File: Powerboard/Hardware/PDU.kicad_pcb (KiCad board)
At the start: 4 copper layers, 60 x 50 mm, 127 parts, among them IC2 SiC437BED-T1-GE3, J1 Conn_01x03_MountingPin, J2 FAN, J3 USB_C_Receptacle_USB2.0, J4 Conn_01x02_Male, J5 Conn_01x08_Male, J6 Conn_01x02_Male, J7 XT60PW-M, J8 Conn_01x04_Male, J9 XT60PW-M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

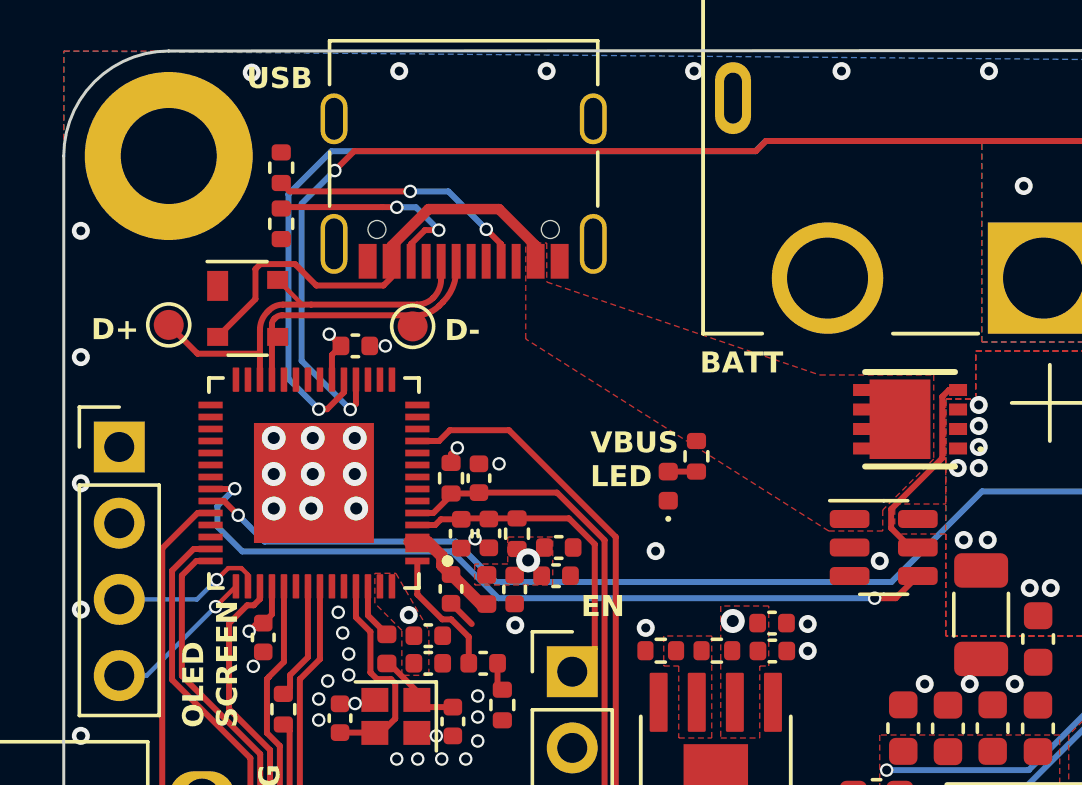
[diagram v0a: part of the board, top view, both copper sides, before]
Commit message: data lines fix
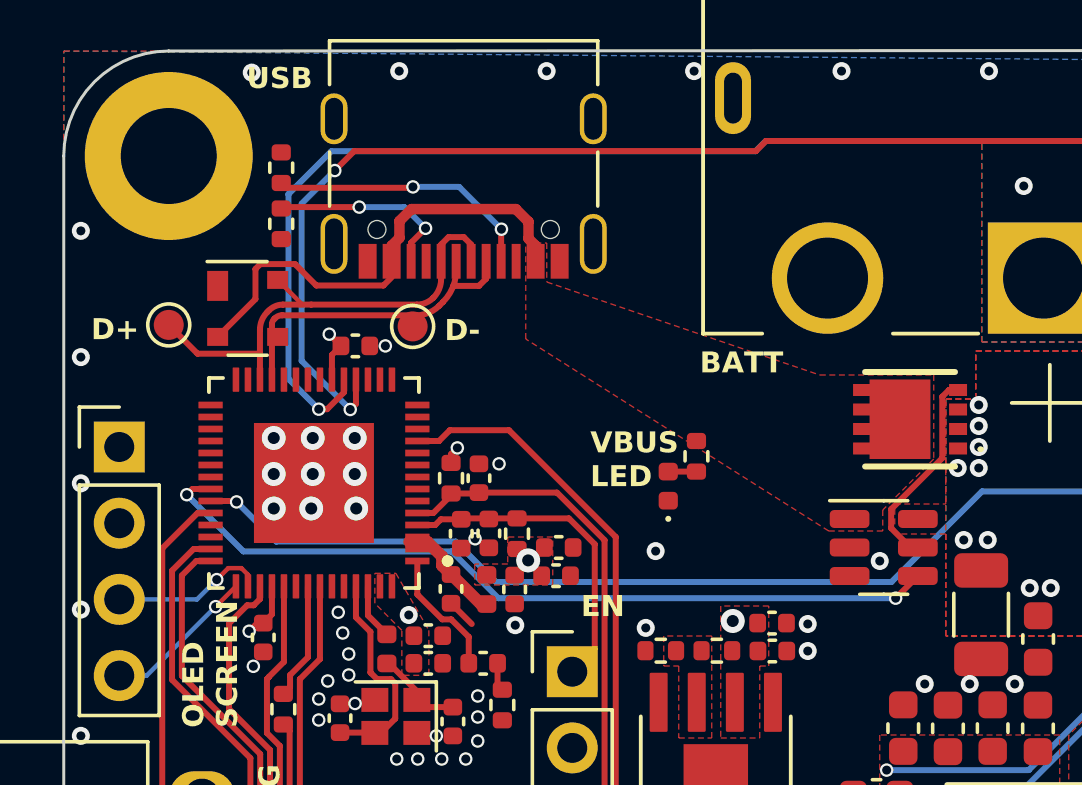
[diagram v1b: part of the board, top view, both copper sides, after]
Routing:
- net /Data+: track 14.2 -> 16.5 mm
- net /Data-: track 9.30 -> 11.1 mm
- net Net-(J3-CC2): track 7.28 -> 6.42 mm
- net VBUS: track 14.6 -> 15.3 mm

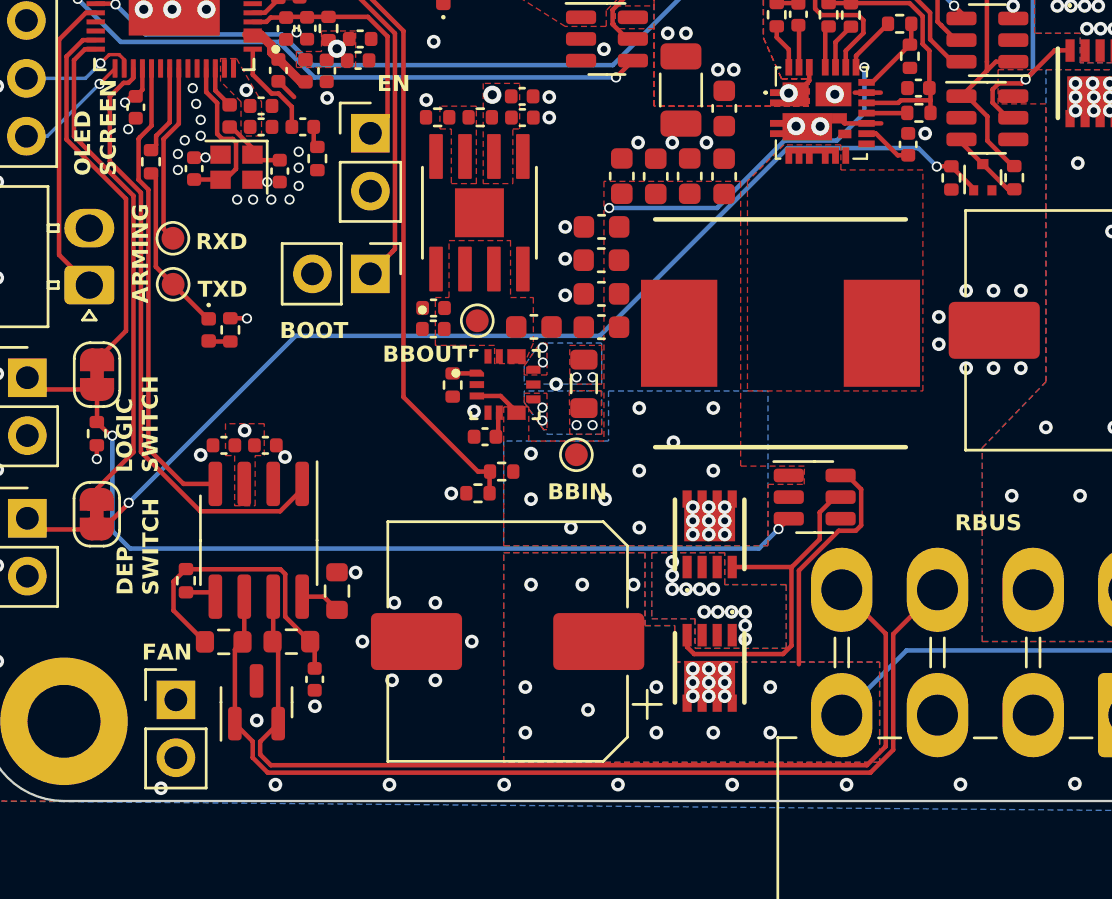
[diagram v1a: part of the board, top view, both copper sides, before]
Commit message: can hardware fix, firmware updates
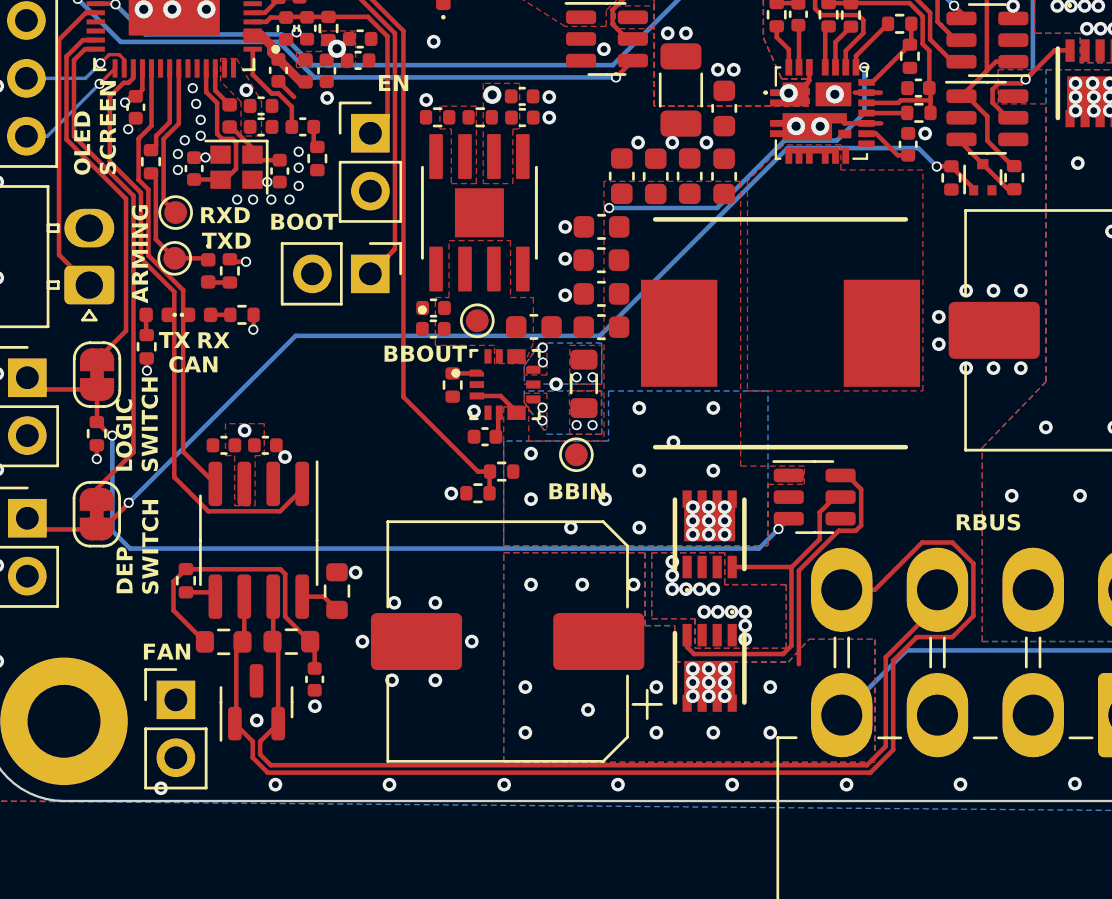
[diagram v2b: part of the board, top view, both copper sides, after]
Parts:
- added CANRXLED1: CANRXLED, LED_SMD:LED_0402_1005Metric, F.Cu at (76.0, 51.7)
- added CANTXLED1: CANTXLED, LED_SMD:LED_0402_1005Metric, F.Cu at (74.1, 51.7)
- added R19: 1k, Resistor_SMD:R_0402_1005Metric, F.Cu at (73.6, 53.1)
- added R36: 1k, Resistor_SMD:R_0402_1005Metric, F.Cu at (77.8, 51.7)
- moved R5 2.59 mm to (77.3, 49.7)
- moved TXLED1 2.59 mm to (76.3, 49.7)
- moved TP4 1.14 mm to (74.9, 49.2)
- moved TP5 1.14 mm to (74.9, 47.2)
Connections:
- J5 pad 7: /CAN- -> /CAN+
- J5 pad 8: /CAN+ -> /CAN-
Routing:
- net /CAN-: track 44.2 -> 53.9 mm
- net /TXD: track 7.45 -> 5.66 mm
- net +3V3: track 6.20 -> 7.42 mm, vias 10 -> 12
- net Net-(U2-U0RXD/PROG/GPIO44): track 7.90 -> 6.82 mm
- net Net-(CANTXLED1-A): track 0.00 -> 0.90 mm
- net Net-(CANRXLED1-A): track 0.00 -> 0.86 mm
- net /CAN_RX: track 20.7 -> 19.9 mm
- net GND: vias 113 -> 112
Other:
- board text added: "CAN"
- board text added: "RX"
- board text added: "TX"

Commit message: v2.1 ordering
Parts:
- 3V3LED1: value 3V3LED -> CYAN_LED
- BATTLED1: value BATT_LED -> ORANGE_LED
- C13, C14: value C -> 11pF
- CANRXLED1: value CANRXLED -> ORANGE_LED
- CANTXLED1: value CANTXLED -> EMERALD_LED
- DEPLED1: value DEP_LED -> RED_LED
- IC2: value SiC437BED-T1-GE3 -> SiC437AED-T1-GE3
- LOGICLED1: value LOGIC_LED -> BLUE_LED
- R12: value 470 -> 5.1k
- TXLED1: value TX_LED -> GREEN_LED
- USBLED1: value USB_LED -> WHITE_LED
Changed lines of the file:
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@@
         (effects (font (size 0.7 0.7) (thickness 0.15)))
     )
-    (fp_text value "SiC437BED-T1-GE3" (at -0.078 -0.068) (layer "F.SilkS") hide
+    (fp_text value "SiC437AED-T1-GE3" (at -0.078 -0.068) (layer "F.SilkS") hide
         (effects (font (size 1.27 1.27) (thickness 0.254)))
     )
@@
     (fp_line (start 10.38 4.22) (end 10.38 -1.72)
       (stroke (width 0.1) (type solid)) (layer "F.Fab"))
-    (pad "1" thru_hole roundrect (at 0 0 180) (size 2.2 1.7) (drill 1.2) (layers "*.Cu" "*.Mask") (roundrect_rratio 0.147059)
+    (pad "1" thru_hole roundrect (at 0 0 180) (size 2.2 1.7) (drill 1.2) (layers "*.Cu" "*.Mask") (roundrect_rratio 0.1470588235)
       (net 16 "/ARMING") (pinfunction "Pin_1") (pintype "passive"))
     (pad "2" thru_hole oval (at 0 2.5 180) (size 2.2 1.7) (drill 1.2) (layers "*.Cu" "*.Mask")
@@
         (effects (font (size 1 1) (thickness 0.15)))
     )
-    (fp_text value "LOGIC_LED" (at 0 1.17 180) (layer "F.Fab")
+    (fp_text value "BLUE_LED" (at 0 1.17 180) (layer "F.Fab")
         (effects (font (size 1 1) (thickness 0.15)))
     )
@@
         (effects (font (size 1 1) (thickness 0.15)))
     )
-    (fp_text value "DEP_LED" (at 0 1.17 180) (layer "F.Fab")
+    (fp_text value "RED_LED" (at 0 1.17 180) (layer "F.Fab")
         (effects (font (size 1 1) (thickness 0.15)))
     )
@@
         (effects (font (size 0.7 0.7) (thickness 0.15)))
     )
-    (fp_text value "USB_LED" (at 0 1.17 90) (layer "F.Fab")
+    (fp_text value "WHITE_LED" (at 0 1.17 90) (layer "F.Fab")
         (effects (font (size 1 1) (thickness 0.15)))
     )
@@
         (effects (font (size 1 1) (thickness 0.15)))
     )
-    (fp_text value "3V3LED" (at 0 1.17 180) (layer "F.Fab")
+    (fp_text value "CYAN_LED" (at 0 1.17 180) (layer "F.Fab")
         (effects (font (size 1 1) (thickness 0.15)))
     )
@@
         (effects (font (size 1 1) (thickness 0.15)))
     )
-    (fp_text value "CANRXLED" (at 0 1.17) (layer "F.Fab")
+    (fp_text value "ORANGE_LED" (at 0 1.17) (layer "F.Fab")
         (effects (font (size 1 1) (thickness 0.15)))
     )
@@
         (effects (font (size 0.7 0.7) (thickness 0.15)))
     )
-    (fp_text value "470" (at 1.546 1.432 -270) (layer "F.Fab")
+    (fp_text value "5.1k" (at 1.546 1.432 -270) (layer "F.Fab")
         (effects (font (size 1 1) (thickness 0.15)))
     )
@@
         (effects (font (size 1 1) (thickness 0.15)))
     )
-    (fp_text value "TX_LED" (at 0 1.17 -90) (layer "F.Fab")
+    (fp_text value "GREEN_LED" (at 0 1.17 -90) (layer "F.Fab")
         (effects (font (size 1 1) (thickness 0.15)))
     )
@@
     (fp_line (start 15.3 -1.1) (end 15.3 -13.9)
       (stroke (width 0.1) (type solid)) (layer "F.Fab"))
-    (pad "1" thru_hole roundrect (at 0 0 180) (size 2.7 3.7) (drill 1.8) (layers "*.Cu" "*.Mask") (roundrect_rratio 0.092593)
+    (pad "1" thru_hole roundrect (at 0 0 180) (size 2.7 3.7) (drill 1.8) (layers "*.Cu" "*.Mask") (roundrect_rratio 0.09259296296)
       (net 3 "GND") (pinfunction "Pin_1") (pintype "passive"))
     (pad "2" thru_hole oval (at 4.2 0 180) (size 2.7 3.7) (drill 1.8) (layers "*.Cu" "*.Mask")
@@
         (effects (font (size 1 1) (thickness 0.15)))
     )
-    (fp_text value "BATT_LED" (at 0 1.17 180) (layer "F.Fab")
+    (fp_text value "ORANGE_LED" (at 0 1.17 180) (layer "F.Fab")
         (effects (font (size 1 1) (thickness 0.15)))
     )
@@
     (fp_line (start 1.6 0.8) (end -1.6 0.8)
       (stroke (width 0.1) (type solid)) (layer "F.Fab"))
-    (pad "1" smd roundrect (at -1.475 0 270) (size 1.15 1.8) (layers "F.Cu" "F.Paste" "F.Mask") (roundrect_rratio 0.217391)
+    (pad "1" smd roundrect (at -1.475 0 270) (size 1.15 1.8) (layers "F.Cu" "F.Paste" "F.Mask") (roundrect_rratio 0.2173913043)
       (net 24 "Net-(IC2-EN)") (pintype "passive"))
-    (pad "2" smd roundrect (at 1.475 0 270) (size 1.15 1.8) (layers "F.Cu" "F.Paste" "F.Mask") (roundrect_rratio 0.217391)
+    (pad "2" smd roundrect (at 1.475 0 270) (size 1.15 1.8) (layers "F.Cu" "F.Paste" "F.Mask") (roundrect_rratio 0.2173913043)
       (net 3 "GND") (pintype "passive"))
     (model "${KICAD6_3DMODEL_DIR}/Capacitor_SMD.3dshapes/C_1206_3216Metric.wrl"
@@
         (effects (font (size 1 1) (thickness 0.15)))
     )
-    (fp_text value "CANTXLED" (at 0 1.17) (layer "F.Fab")
+    (fp_text value "EMERALD_LED" (at 0 1.17) (layer "F.Fab")
         (effects (font (size 1 1) (thickness 0.15)))
     )
@@
         (effects (font (size 1 1) (thickness 0.15)))
     )
-    (fp_text value "C" (at 0 1.16 90) (layer "F.Fab")
+    (fp_text value "11pF" (at 0 1.16 90) (layer "F.Fab")
         (effects (font (size 1 1) (thickness 0.15)))
     )
@@
         (effects (font (size 1 1) (thickness 0.15)))
     )
-    (fp_text value "C" (at 0 1.16 90) (layer "F.Fab")
+    (fp_text value "11pF" (at 0 1.16 90) (layer "F.Fab")
         (effects (font (size 1 1) (thickness 0.15)))
     )
